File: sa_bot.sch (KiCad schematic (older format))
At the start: 60 parts, among them CON1 MicroSD_Card, P1 USB_OTG, P11 MOTOR_A, P12 MOTOR_B, P13 SONAR_4, P14 SONAR_2, P15 SONAR_3, P17 DBG_CONN, P18 CONN_01X04, P2 BatteryHolder, P3 IR4_JMP, P4 IR2_JMP, P5 IR3_JMP, P6 ExPower, P7 IR_4, P8 IR_2, P9 IR_3, Q1 Q_PMOS_DSG, SW1 SWITCH_INV, SW2 SW_PUSH, SW3 SW_PUSH, U1 74AHC1G125, U2 SAMD21G18, U3 AP2112K-3.3V, U4 NCP1402, U5 DRV8835, Y1 Crystal_Small

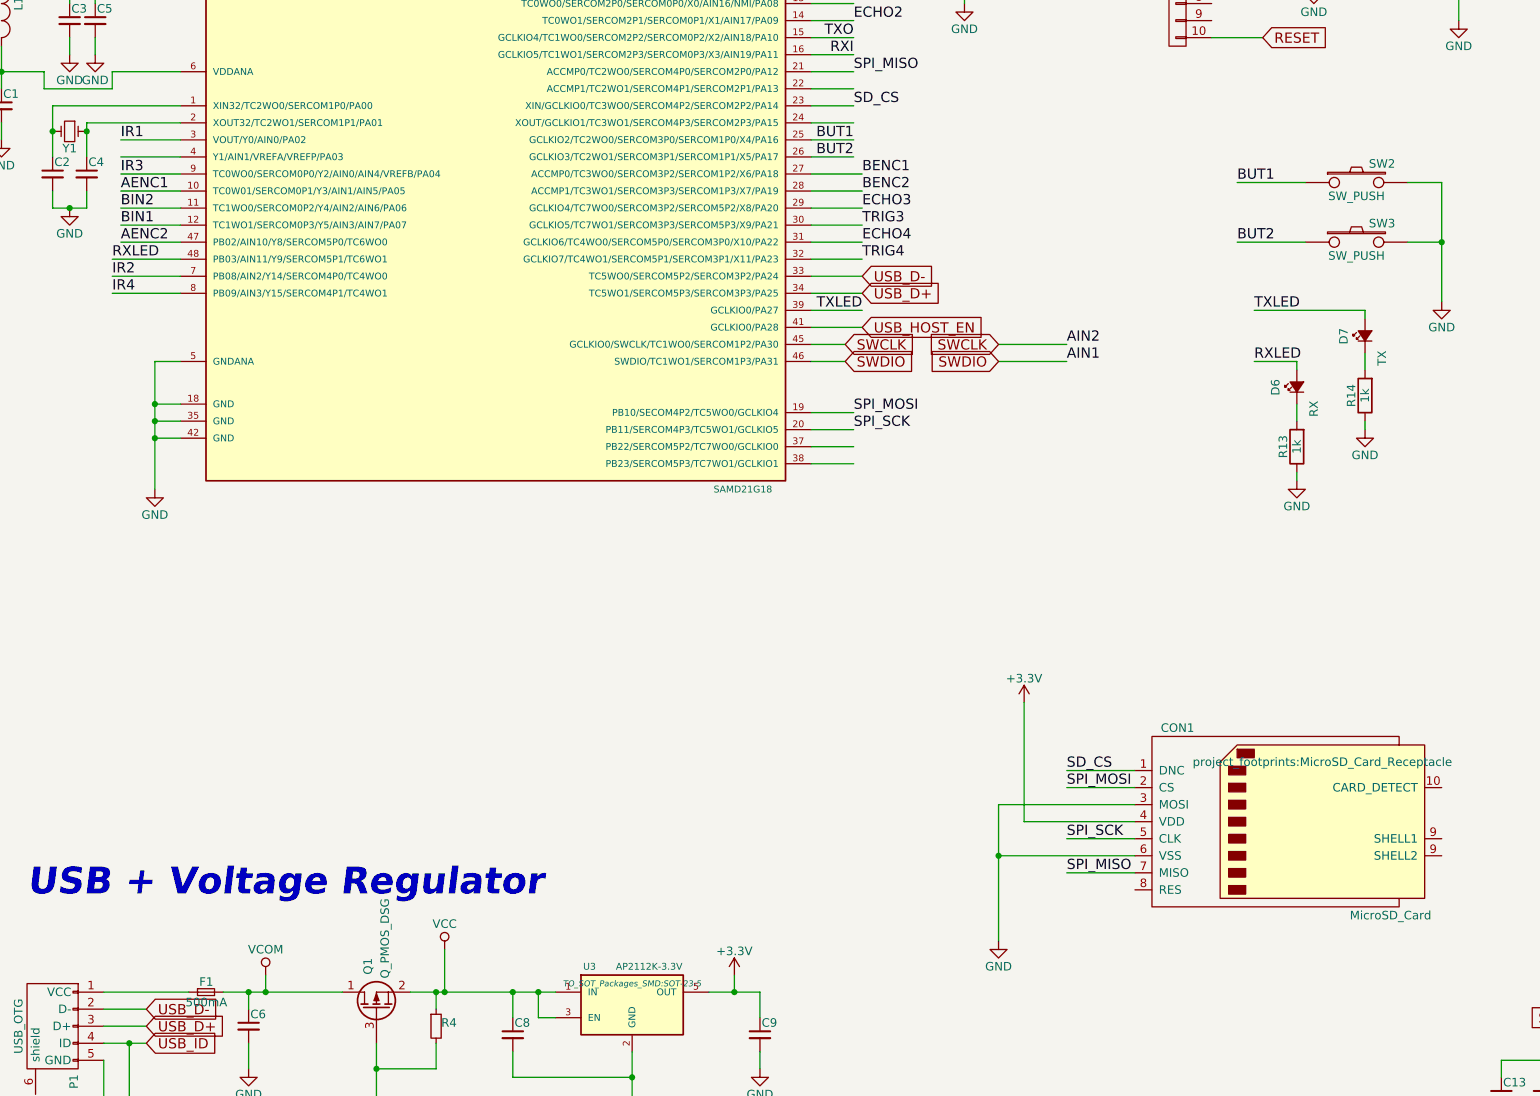
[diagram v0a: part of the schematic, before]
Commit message: Moved RXTX LEDs
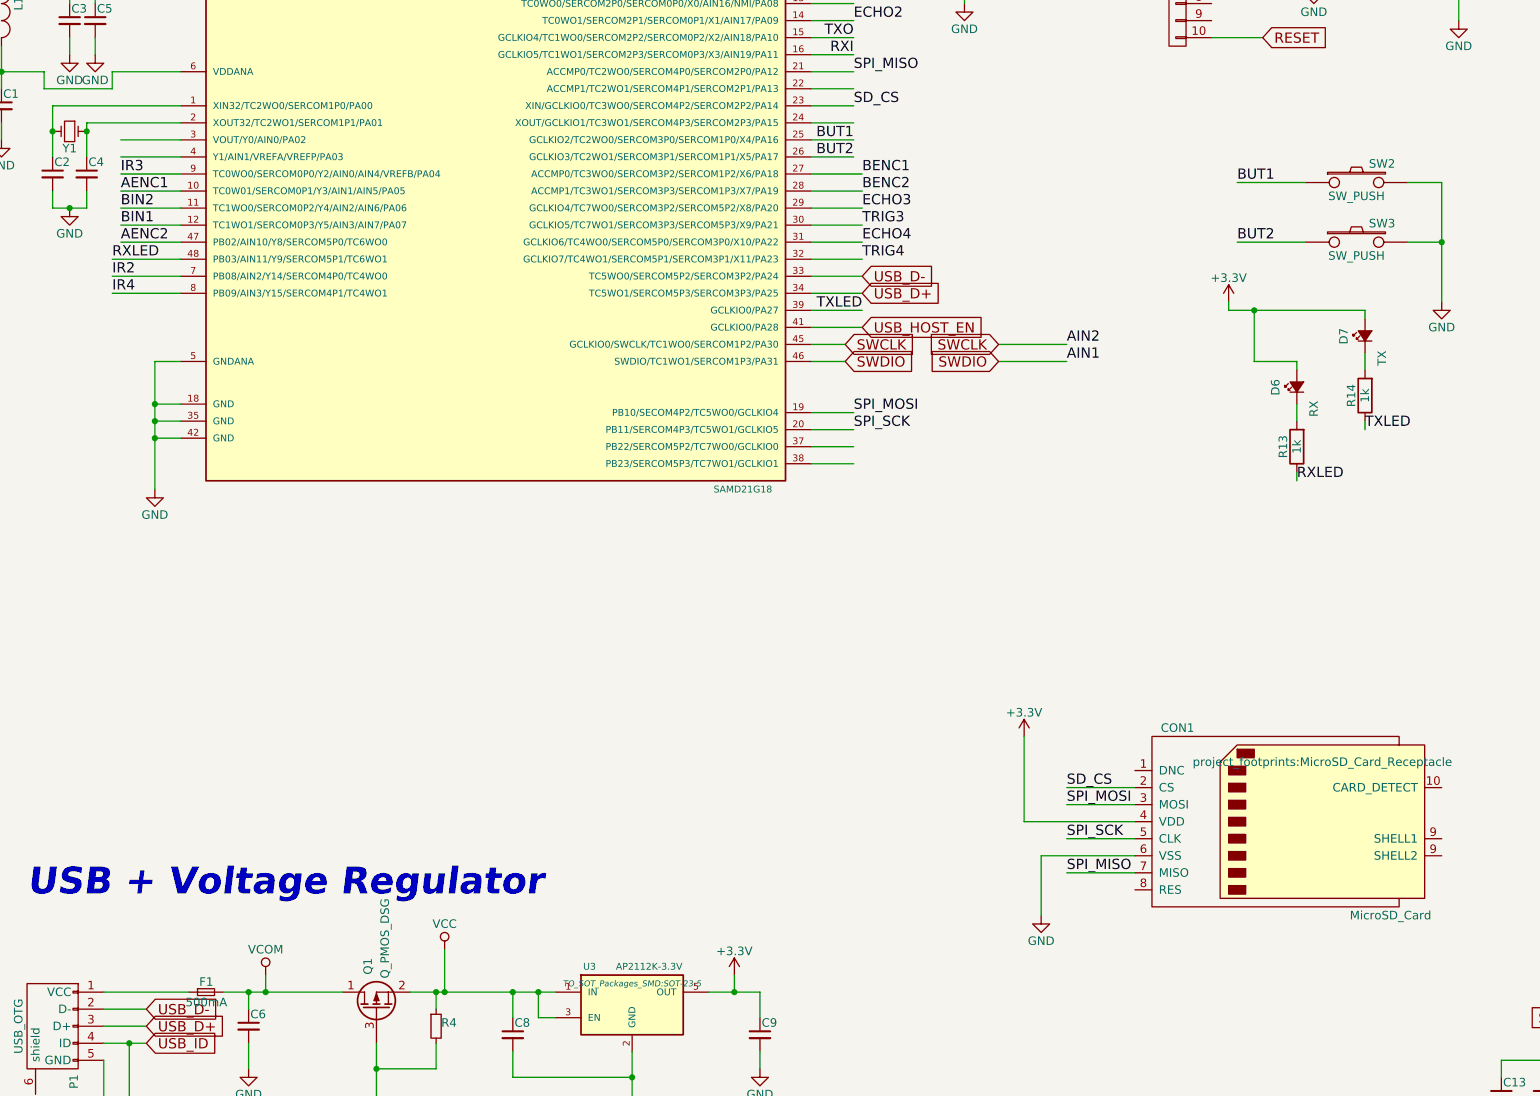
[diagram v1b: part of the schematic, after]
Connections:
- net +3V3: now also D6.2 (A), D7.2 (A)
- net GND: no longer CON1.3 (MOSI), R13.1, R14.1
- net RXLED: now also R13.1; no longer D6.2 (A)
- net SD_CS: now also CON1.2 (CS); no longer CON1.1 (DNC)
- net SPI_MOSI: now also CON1.3 (MOSI); no longer CON1.2 (CS)
- net TXLED: now also R14.1; no longer D7.2 (A)
- net IR1: no longer names the net of U2.3 (VOUT/Y0/AIN0/PA02)
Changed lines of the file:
@@
 Text Label 10500 8450 0    60   ~ 0
 BM2
-Text Label 1950 2650 0    60   ~ 0
-IR1
 Text Label 1900 3450 0    60   ~ 0
 IR2
@@
 $EndComp
 $Comp
-L GND #PWR042
-U 1 1 57070FCB
-P 9250 4350
-F 0 "#PWR042" H 9250 4100 50  0001 C CNN
-F 1 "GND" H 9250 4200 50  0000 C CNN
-F 2 "" H 9250 4350 60  0000 C CNN
-F 3 "" H 9250 4350 60  0000 C CNN
-	1    9250 4350
-	1    0    0    -1
-$EndComp
-$Comp
 L Led_Small D6
 U 1 1 5707109B
@@
 	-1   0    0    1
 $EndComp
-$Comp
-L GND #PWR043
-U 1 1 570710A9
-P 8850 4650
-F 0 "#PWR043" H 8850 4400 50  0001 C CNN
-F 1 "GND" H 8850 4500 50  0000 C CNN
-F 2 "" H 8850 4650 60  0000 C CNN
-F 3 "" H 8850 4650 60  0000 C CNN
-	1    8850 4650
-	1    0    0    -1
-$EndComp
-Text Label 8600 3650 0    60   ~ 0
+Text Label 9250 4350 0    60   ~ 0
 TXLED
-Text Label 8600 3950 0    60   ~ 0
+Text Label 8850 4650 0    60   ~ 0
 RXLED
 Text Label 6250 4350 0    60   ~ 0
@@
 Text Label 6250 2250 0    60   ~ 0
 SPI_MISO
-Text Label 7500 6350 0    60   ~ 0
+Text Label 7500 6450 0    60   ~ 0
 SD_CS
-Text Label 7500 6450 0    60   ~ 0
+Text Label 7500 6550 0    60   ~ 0
 SPI_MOSI
 Text Label 7500 6750 0    60   ~ 0
@@
 SPI_MISO
 $Comp
-L GND #PWR044
+L GND #PWR042
 U 1 1 57075848
-P 7100 7350
-F 0 "#PWR044" H 7100 7100 50  0001 C CNN
-F 1 "GND" H 7100 7200 50  0000 C CNN
-F 2 "" H 7100 7350 60  0000 C CNN
-F 3 "" H 7100 7350 60  0000 C CNN
-	1    7100 7350
-	1    0    0    -1
-$EndComp
-$Comp
-L +3.3V #PWR045
+P 7350 7200
+F 0 "#PWR042" H 7350 6950 50  0001 C CNN
+F 1 "GND" H 7350 7050 50  0000 C CNN
+F 2 "" H 7350 7200 60  0000 C CNN
+F 3 "" H 7350 7200 60  0000 C CNN
+	1    7350 7200
+	1    0    0    -1
+$EndComp
+$Comp
+L +3.3V #PWR043
 U 1 1 57075928
-P 7250 5950
-F 0 "#PWR045" H 7250 5800 50  0001 C CNN
-F 1 "+3.3V" H 7250 6090 50  0000 C CNN
-F 2 "" H 7250 5950 60  0000 C CNN
-F 3 "" H 7250 5950 60  0000 C CNN
-	1    7250 5950
+P 7250 6150
+F 0 "#PWR043" H 7250 6000 50  0001 C CNN
+F 1 "+3.3V" H 7250 6290 50  0000 C CNN
+F 2 "" H 7250 6150 60  0000 C CNN
+F 3 "" H 7250 6150 60  0000 C CNN
+	1    7250 6150
 	1    0    0    -1
 $EndComp
@@
 $EndComp
 $Comp
-L +5V #PWR046
+L +5V #PWR044
 U 1 1 57084A79
 P 9800 1100
-F 0 "#PWR046" H 9800 950 50  0001 C CNN
+F 0 "#PWR044" H 9800 950 50  0001 C CNN
 F 1 "+5V" H 9800 1240 50  0000 C CNN
 F 2 "" H 9800 1100 60  0000 C CNN
@@
 $EndComp
 $Comp
-L GND #PWR047
+L GND #PWR045
 U 1 1 57084B5C
 P 9800 1950
-F 0 "#PWR047" H 9800 1700 50  0001 C CNN
+F 0 "#PWR045" H 9800 1700 50  0001 C CNN
 F 1 "GND" H 9800 1800 50  0000 C CNN
 F 2 "" H 9800 1950 60  0000 C CNN
@@
 	2300 3350 1900 3350
 Wire Wire Line
-	8600 3650 9250 3650
+	8450 3650 9250 3650
 Wire Wire Line
 	9250 3650 9250 3700
@@
 	6000 2250 6250 2250
 Wire Wire Line
-	7900 6350 7500 6350
-Wire Wire Line
 	7900 6450 7500 6450
 Wire Wire Line
-	7900 6550 7100 6550
-Wire Wire Line
-	7100 6550 7100 7350
-Wire Wire Line
-	7900 6650 7250 6650
-Wire Wire Line
-	7250 6650 7250 5950
+	7250 6650 7900 6650
 Wire Wire Line
 	7900 6750 7500 6750
 Wire Wire Line
-	7900 6850 7100 6850
-Connection ~ 7100 6850
+	7350 6850 7900 6850
 Wire Wire Line
 	7900 6950 7500 6950
@@
 HVECHO2
 $Comp
-L GND #PWR048
+L GND #PWR046
 U 1 1 5725CCD1
 P 12700 2250
-F 0 "#PWR048" H 12700 2000 50  0001 C CNN
+F 0 "#PWR046" H 12700 2000 50  0001 C CNN
 F 1 "GND" H 12700 2100 50  0000 C CNN
 F 2 "" H 12700 2250 60  0000 C CNN
@@
 HVECHO3
 $Comp
-L GND #PWR049
+L GND #PWR047
 U 1 1 57261D7C
 P 13550 2300
-F 0 "#PWR049" H 13550 2050 50  0001 C CNN
+F 0 "#PWR047" H 13550 2050 50  0001 C CNN
 F 1 "GND" H 13550 2150 50  0000 C CNN
 F 2 "" H 13550 2300 60  0000 C CNN
@@
 HVECHO4
 $Comp
-L GND #PWR050
+L GND #PWR048
 U 1 1 57261E31
 P 14550 2300
-F 0 "#PWR050" H 14550 2050 50  0001 C CNN
+F 0 "#PWR048" H 14550 2050 50  0001 C CNN
 F 1 "GND" H 14550 2150 50  0000 C CNN
 F 2 "" H 14550 2300 60  0000 C CNN
@@
 SBATT
 $Comp
-L GND #PWR051
+L GND #PWR049
 U 1 1 572762E5
 P 7700 10800
-F 0 "#PWR051" H 7700 10800 30  0001 C CNN
+F 0 "#PWR049" H 7700 10800 30  0001 C CNN
 F 1 "GND" H 7700 10730 30  0001 C CNN
 F 2 "" H 7700 10800 60  0000 C CNN
@@
 $EndComp
 $Comp
-L VCC #PWR052
+L VCC #PWR050
 U 1 1 572763A4
 P 7950 10200
-F 0 "#PWR052" H 7950 10050 50  0001 C CNN
+F 0 "#PWR050" H 7950 10050 50  0001 C CNN
 F 1 "VCC" H 7950 10350 50  0000 C CNN
 F 2 "" H 7950 10200 60  0000 C CNN
@@
 Text Label 5850 10350 2    60   ~ 0
 NC
+Wire Wire Line
+	7900 6550 7500 6550
+Wire Wire Line
+	7250 6150 7250 6650
+Wire Wire Line
+	7350 6850 7350 7200
+$Comp
+L +3.3V #PWR051
+U 1 1 578975FF
+P 8450 3600
+F 0 "#PWR051" H 8450 3450 50  0001 C CNN
+F 1 "+3.3V" H 8450 3740 50  0000 C CNN
+F 2 "" H 8450 3600 60  0000 C CNN
+F 3 "" H 8450 3600 60  0000 C CNN
+	1    8450 3600
+	1    0    0    -1
+$EndComp
+Wire Wire Line
+	8450 3650 8450 3600
+Wire Wire Line
+	8600 3950 8600 3650
+Connection ~ 8600 3650
 $EndSCHEMATC

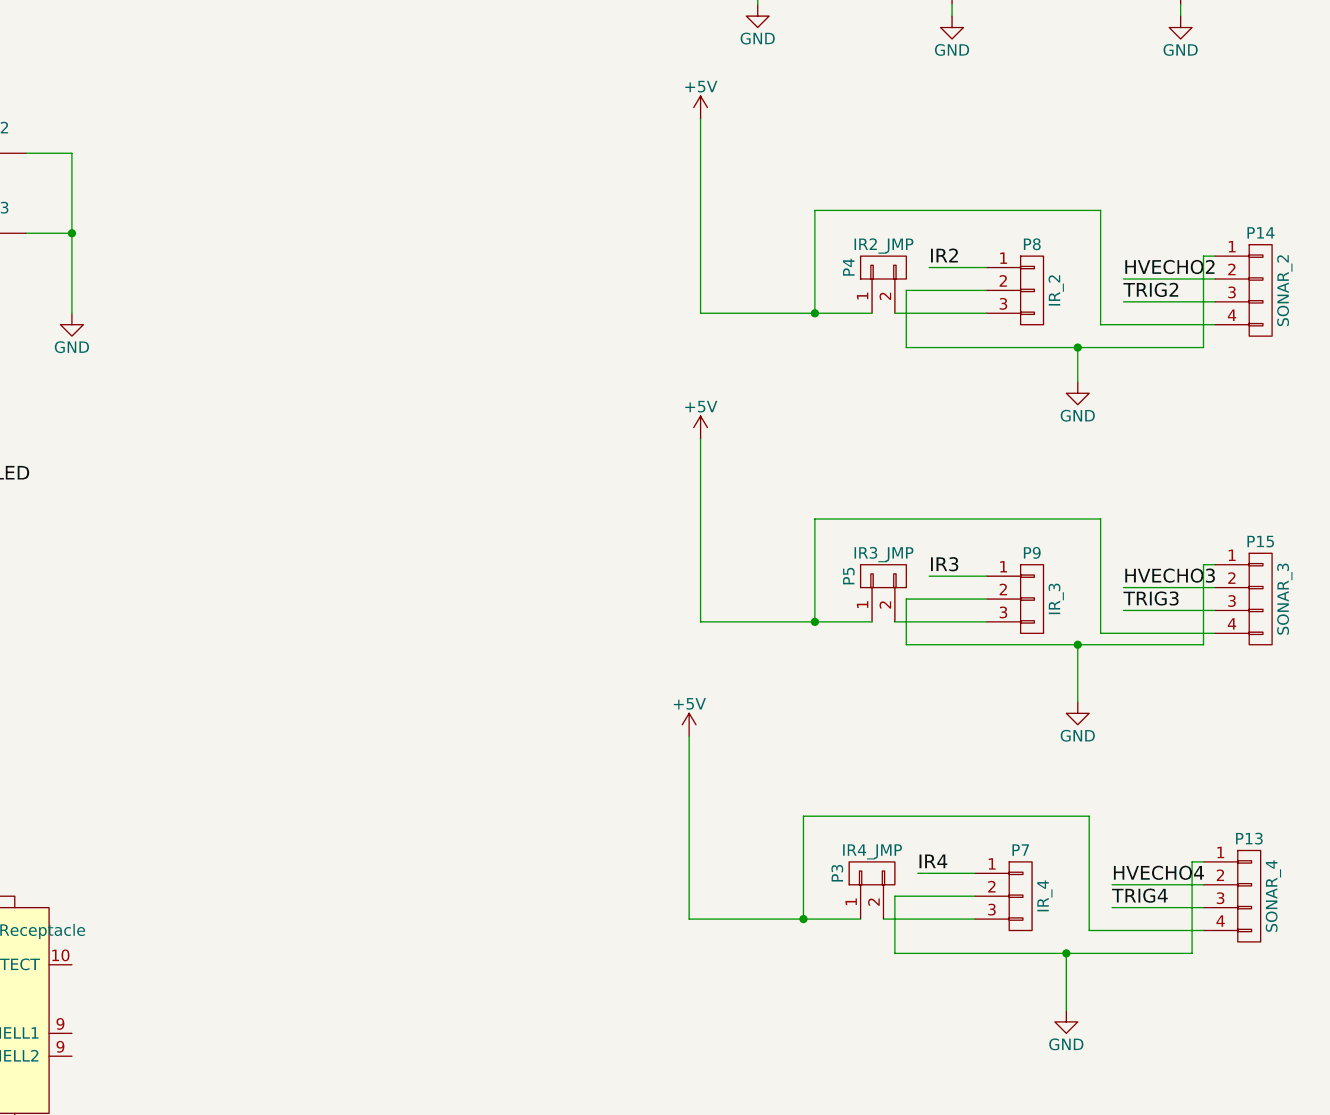
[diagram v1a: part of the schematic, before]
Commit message: Added Reset Button
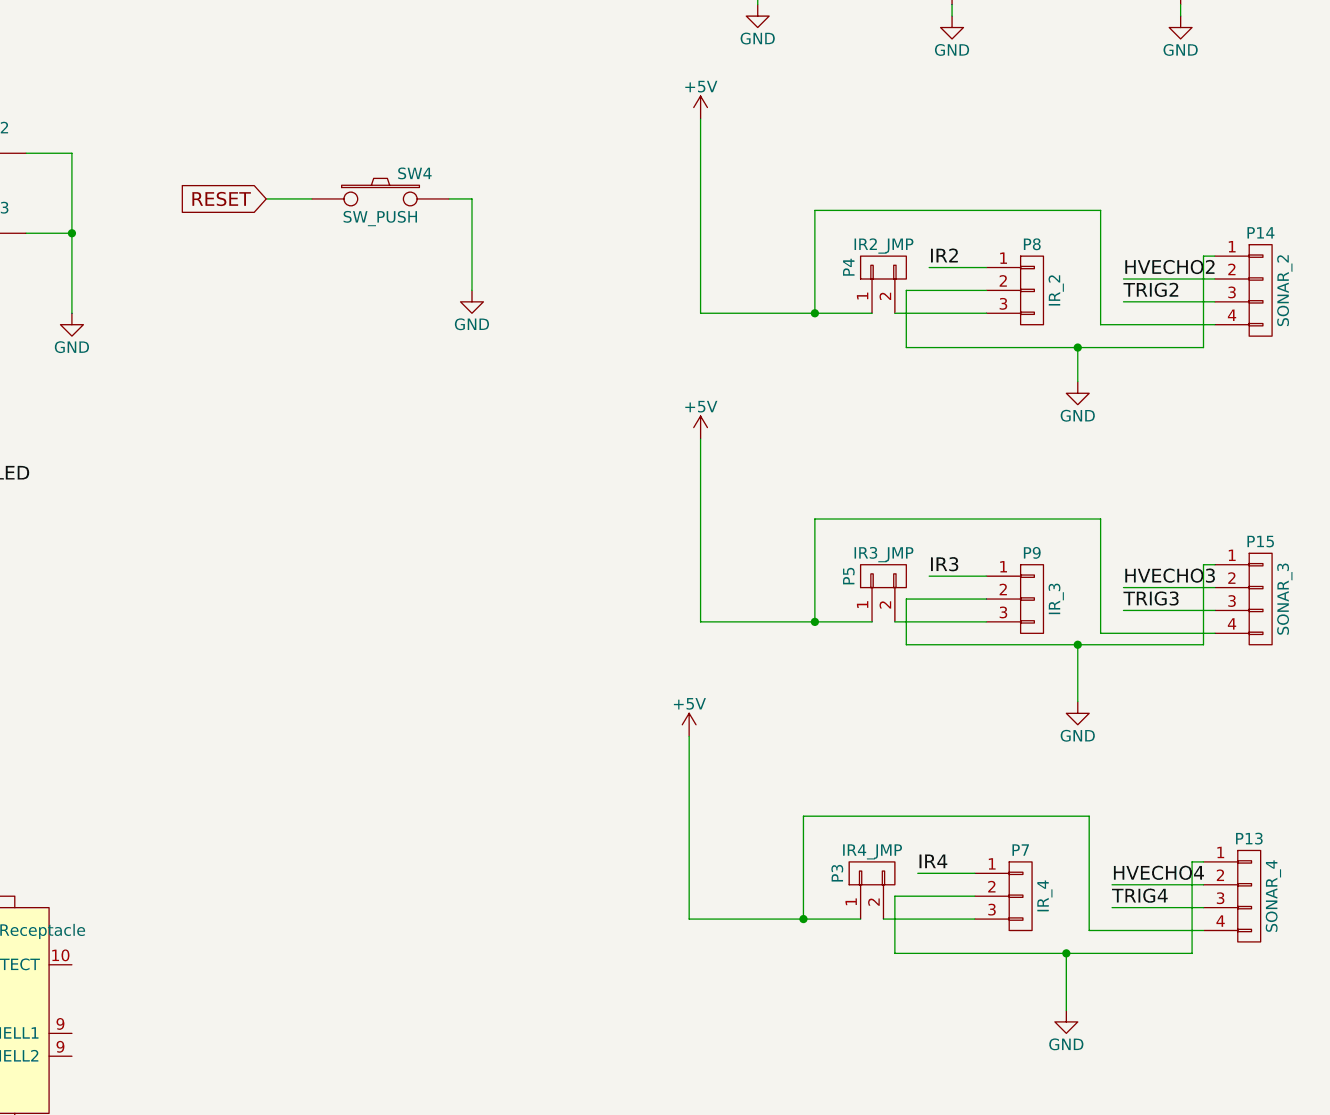
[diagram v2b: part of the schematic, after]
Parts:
- added SW4: SW_PUSH, Buttons_Switches_SMD:SW_SPST_EVQPE1, symbol SW_PUSH
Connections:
- net GND: now also SW4.2
- net RESET: now also SW4.1
